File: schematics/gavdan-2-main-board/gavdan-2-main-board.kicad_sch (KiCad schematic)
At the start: 25 parts

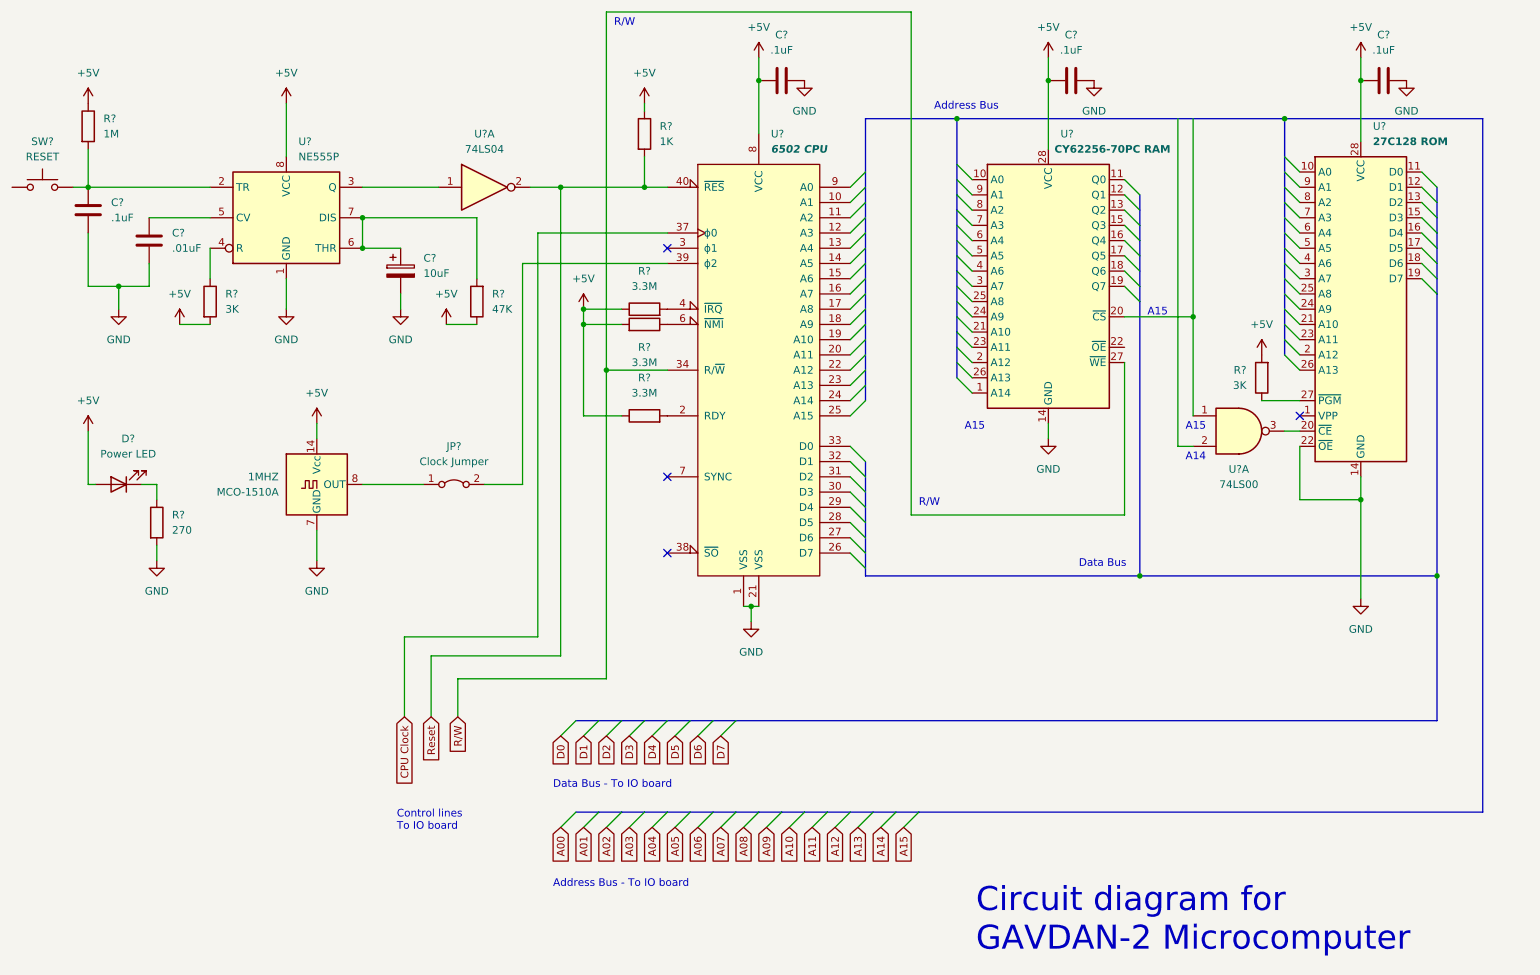
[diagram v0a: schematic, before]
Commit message: Updates to schematics to correct errors
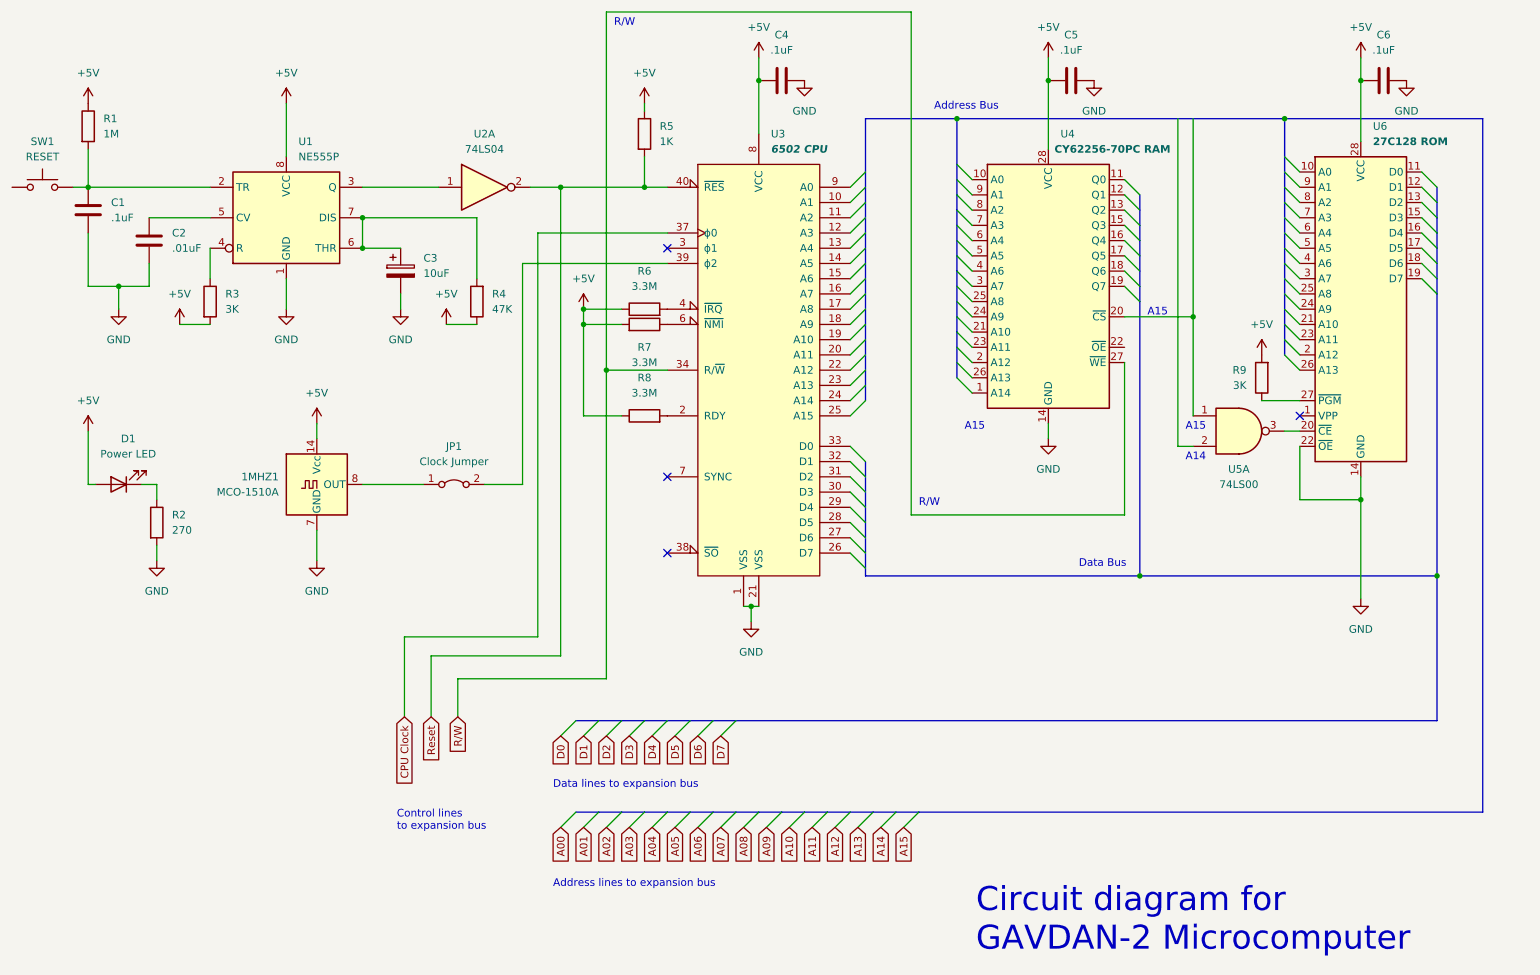
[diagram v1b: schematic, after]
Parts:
- gave numbers to parts that had none: 24
- renumbered 1MHZ to 1MHZ1
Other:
- note added: "Address lines to expansion bus"
- note added: "Control lines to expansion bus"
- note added: "Data lines to expansion bus"
- note removed: "Address Bus - To IO board"
- note removed: "Control lines To IO board"
- note removed: "Data Bus - To IO board"
